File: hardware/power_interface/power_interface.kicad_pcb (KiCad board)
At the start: 2 copper layers, 96 x 64 mm, 64 parts, among them J1 PJ-102AH, J2 BIAS_EN, J3 B10B-XH-A, J4 B10B-XH-A, J5 TSW-106-08-G-D-RA, U1 TLV75533PDBVR, U2 MAX5026EUT+T, U3 MCP3202-BI/SN

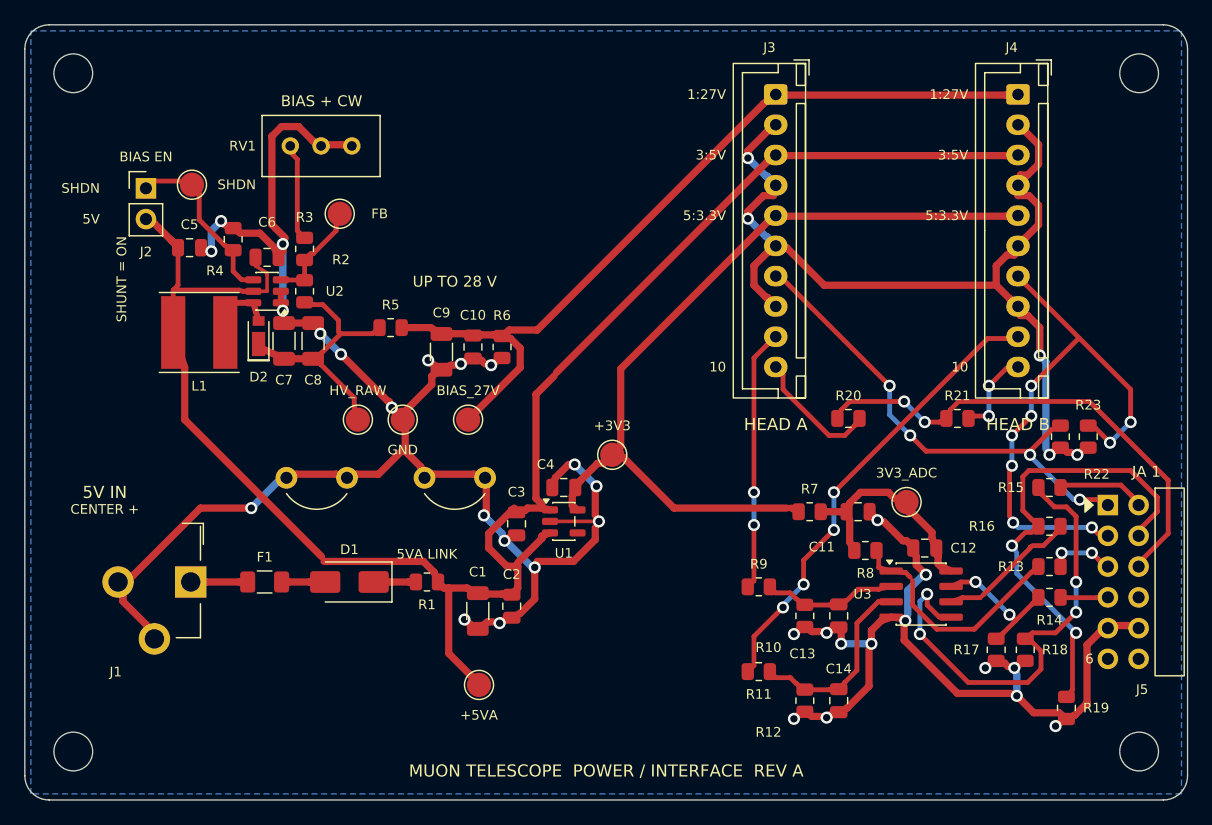
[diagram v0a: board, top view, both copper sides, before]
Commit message: accepting track power repair. Need to do for the same for head
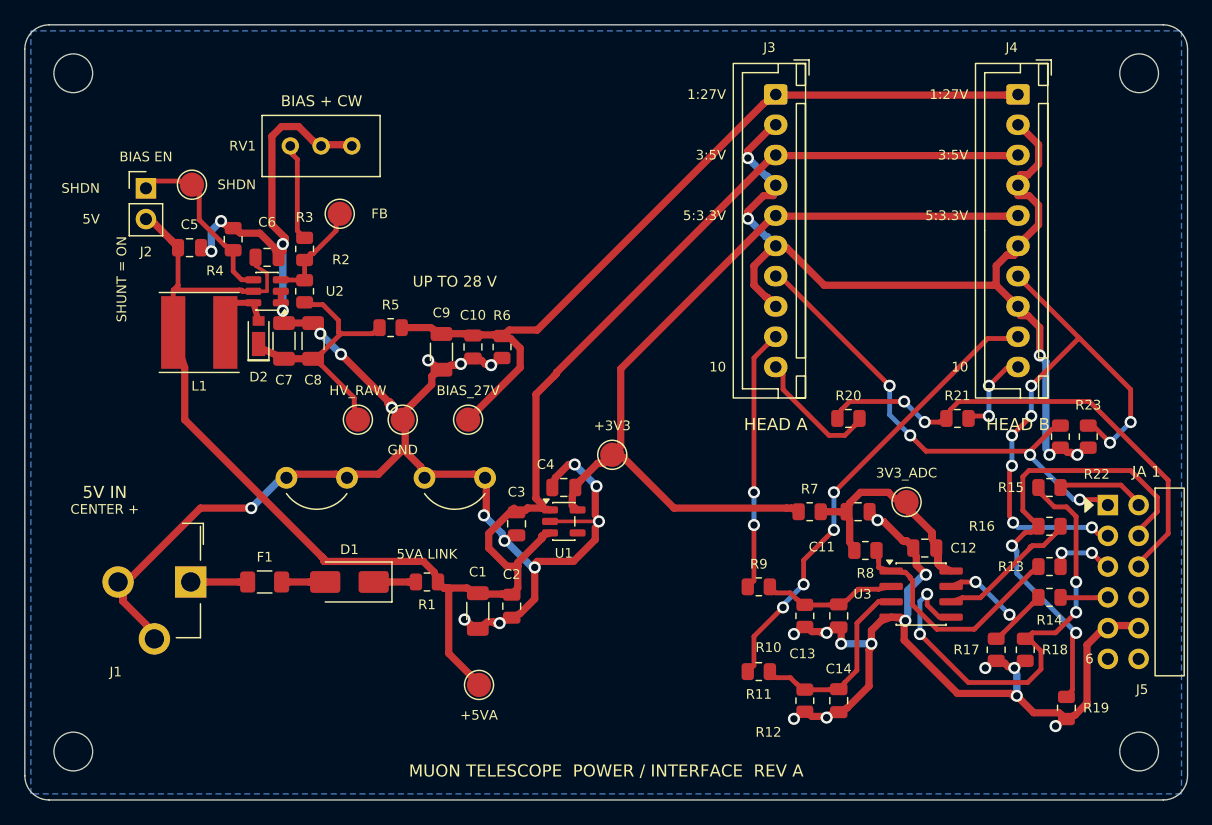
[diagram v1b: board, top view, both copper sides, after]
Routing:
- net GND: track 285.1 -> 298.2 mm
- net /+5VA: track 141.4 -> 144.9 mm
- net /+3V3_ADC: track 18.7 -> 20.9 mm
- net /+3V3_LOCAL: track 67.6 -> 68.5 mm
- net /ADC_MISO: track 11.1 -> 11.9 mm
- net /ADC_CS_N: track 19.4 -> 20.1 mm
- net /JA_MISO: track 38.0 -> 38.8 mm

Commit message: updated  docs, called everything a pass, used v0 version number. The files need to go to pcbway now.
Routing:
- net GND: track 298.2 -> 295.4 mm
- net /+3V3_ADC: track 20.9 -> 19.0 mm
- net /+3V3_LOCAL: track 68.5 -> 68.0 mm
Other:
- board text added: "MUON TELESCOPE POWER / INTERFACE v0 2026-09-18"
- board text removed: "MUON TELESCOPE POWER / INTERFACE REV A"
